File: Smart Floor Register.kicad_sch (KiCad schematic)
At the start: 0 parts

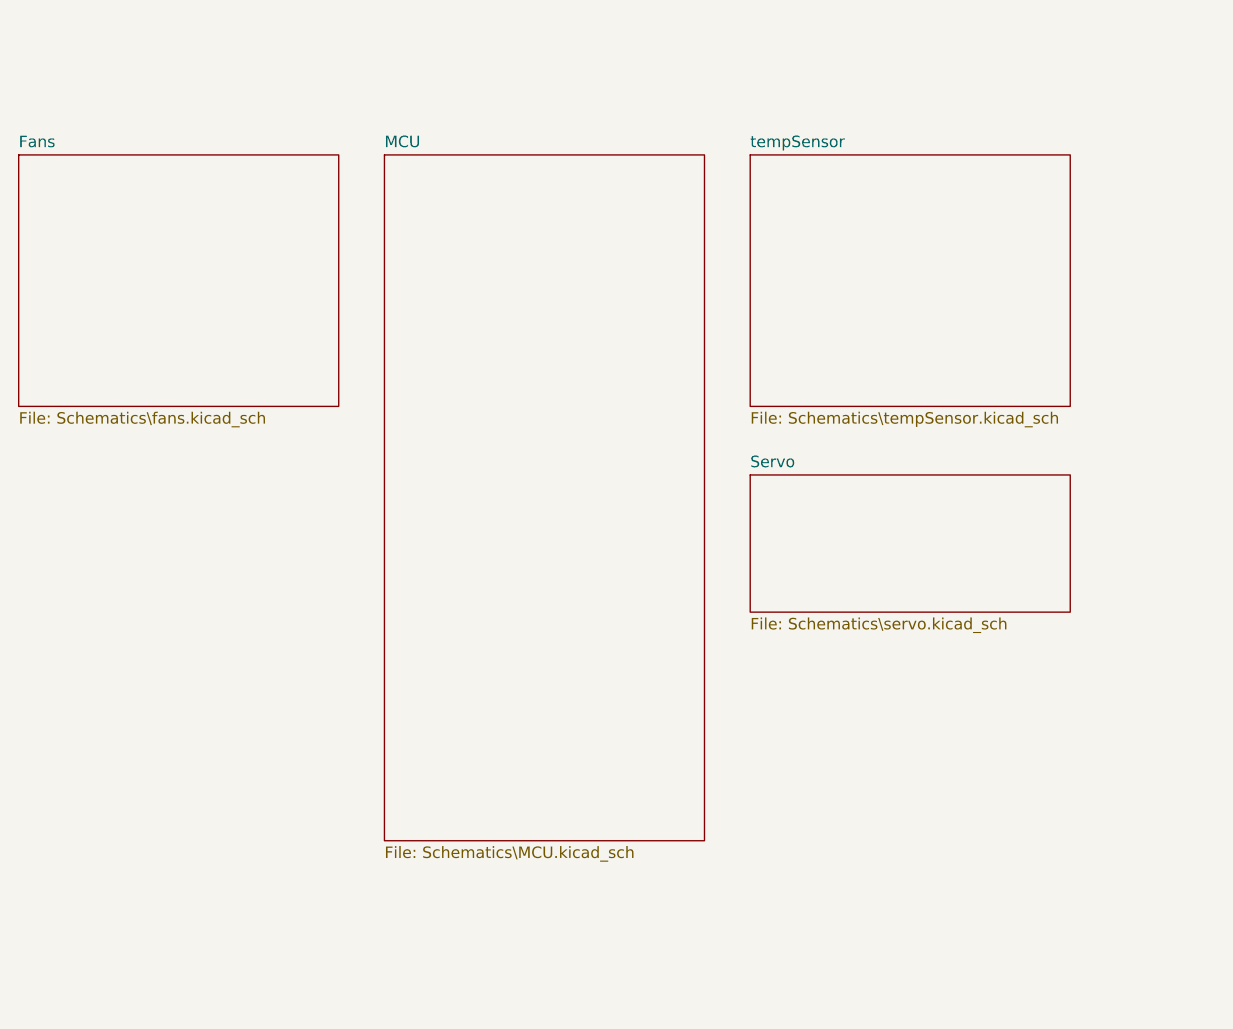
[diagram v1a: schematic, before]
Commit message: Add MCU circuit
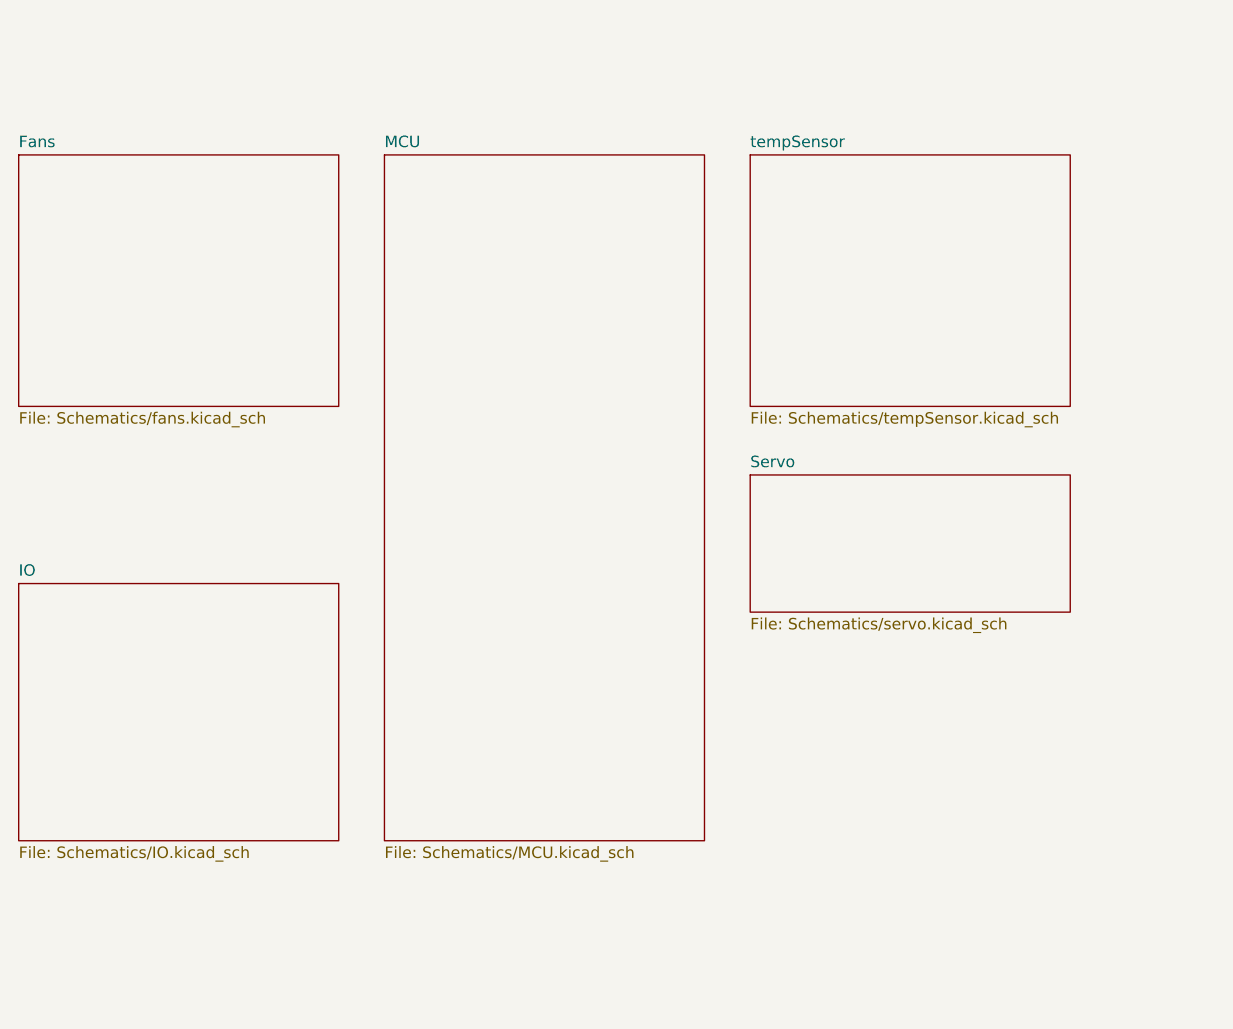
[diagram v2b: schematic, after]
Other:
- added sheet IO (Schematics/IO.kicad_sch)
- sheet Fans: file Schematics\fans.kicad_sch -> Schematics/fans.kicad_sch
- sheet MCU: file Schematics\MCU.kicad_sch -> Schematics/MCU.kicad_sch
- sheet Servo: file Schematics\servo.kicad_sch -> Schematics/servo.kicad_sch
- sheet tempSensor: file Schematics\tempSensor.kicad_sch -> Schematics/tempSensor.kicad_sch
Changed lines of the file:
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@@
       (effects (font (size 1.27 1.27)) (justify left bottom))
     )
-    (property "Sheet file" "Schematics\\servo.kicad_sch" (id 1) (at 165.1 114.8846 0)
+    (property "Sheet file" "Schematics/servo.kicad_sch" (id 1) (at 165.1 114.8846 0)
       (effects (font (size 1.27 1.27)) (justify left top))
     )
@@
       (effects (font (size 1.27 1.27)) (justify left bottom))
     )
-    (property "Sheet file" "Schematics\\MCU.kicad_sch" (id 1) (at 124.46 140.2846 0)
+    (property "Sheet file" "Schematics/MCU.kicad_sch" (id 1) (at 124.46 140.2846 0)
       (effects (font (size 1.27 1.27)) (justify left top))
     )
@@
       (effects (font (size 1.27 1.27)) (justify left bottom))
     )
-    (property "Sheet file" "Schematics\\tempSensor.kicad_sch" (id 1) (at 165.1 92.0246 0)
+    (property "Sheet file" "Schematics/tempSensor.kicad_sch" (id 1) (at 165.1 92.0246 0)
+      (effects (font (size 1.27 1.27)) (justify left top))
+    )
+  )
+  (sheet (at 83.82 111.125) (size 35.56 28.575) (fields_autoplaced)
+    (stroke (width 0.1524) (type solid) (color 0 0 0 0))
+    (fill (color 0 0 0 0.0000))
+    (property "Sheet name" "IO" (id 0) (at 83.82 110.4134 0)
+      (effects (font (size 1.27 1.27)) (justify left bottom))
+    )
+    (property "Sheet file" "Schematics/IO.kicad_sch" (id 1) (at 83.82 140.2846 0)
       (effects (font (size 1.27 1.27)) (justify left top))
     )
@@
       (effects (font (size 1.27 1.27)) (justify left bottom))
     )
-    (property "Sheet file" "Schematics\\fans.kicad_sch" (id 1) (at 83.82 92.0246 0)
+    (property "Sheet file" "Schematics/fans.kicad_sch" (id 1) (at 83.82 92.0246 0)
       (effects (font (size 1.27 1.27)) (justify left top))
     )
@@
     (path "/3b809d5e-1cd6-4bd7-8775-d6e8648b017c" (page "4"))
     (path "/ed227731-8e20-48d6-ab3d-3bb44546ae2c" (page "5"))
+    (path "/e5852d82-8ff6-4012-ac66-763fa215a023" (page "6"))
   )
   (symbol_instances
+    (path "/49126cb1-3295-4f9c-ba5a-a7f1d530269a/0ba5132d-9905-4101-b8fb-d13fd8eb3278"
+      (reference "#PWR?") (unit 1) (value "VCC") (footprint "")
+    )
+    (path "/49126cb1-3295-4f9c-ba5a-a7f1d530269a/33b8dcc0-1a9b-40a0-97ec-c23023a23c96"
+      (reference "#PWR?") (unit 1) (value "Earth") (footprint "")
+    )
+    (path "/49126cb1-3295-4f9c-ba5a-a7f1d530269a/72c0072b-392e-4e7f-97f5-dd28eacd0e25"
+      (reference "#PWR?") (unit 1) (value "Earth") (footprint "")
+    )
+    (path "/49126cb1-3295-4f9c-ba5a-a7f1d530269a/781801cc-7cbe-41ec-88cd-6260168418c2"
+      (reference "#PWR?") (unit 1) (value "Earth") (footprint "")
+    )
+    (path "/49126cb1-3295-4f9c-ba5a-a7f1d530269a/c2f2a113-ef08-4a50-83fd-9e527d0d90f6"
+      (reference "#PWR?") (unit 1) (value "VCC") (footprint "")
+    )
+    (path "/e5852d82-8ff6-4012-ac66-763fa215a023/df26c841-4ff3-4cde-959c-1d6a7c88c93e"
+      (reference "#PWR?") (unit 1) (value "Earth") (footprint "")
+    )
+    (path "/49126cb1-3295-4f9c-ba5a-a7f1d530269a/027587c6-5a8d-4b56-aa6d-ac51c1c0279d"
+      (reference "C?") (unit 1) (value "1uF") (footprint "")
+    )
+    (path "/49126cb1-3295-4f9c-ba5a-a7f1d530269a/317cf53b-7c2d-48ed-ac0b-c02d04fc9aba"
+      (reference "C?") (unit 1) (value "1uF") (footprint "")
+    )
+    (path "/49126cb1-3295-4f9c-ba5a-a7f1d530269a/645e38cc-aaf0-425a-9ead-62a84a8ca331"
+      (reference "C?") (unit 1) (value "1uF") (footprint "")
+    )
+    (path "/e5852d82-8ff6-4012-ac66-763fa215a023/b59f5cd4-3d0b-4837-87b8-455eb74be610"
+      (reference "J?") (unit 1) (value "USB_B_Micro") (footprint "")
+    )
     (path "/49126cb1-3295-4f9c-ba5a-a7f1d530269a/9aa4051b-5d8e-420b-bd92-028862775303"
       (reference "U?") (unit 1) (value "ATmega32U4-M") (footprint "Package_DFN_QFN:QFN-44-1EP_7x7mm_P0.5mm_EP5.2x5.2mm")
     )
+    (path "/49126cb1-3295-4f9c-ba5a-a7f1d530269a/6e0cb104-c4a0-43c8-bedf-8a80f0d18d8f"
+      (reference "Y?") (unit 1) (value "16MHz ") (footprint "")
+    )
   )

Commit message: Motor Controllers
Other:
- added sheet Power (Schematics/power.kicad_sch)
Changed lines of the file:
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@@
 (kicad_sch (version 20211123) (generator eeschema)
   (paper "A4")
-  (sheet (at 165.1 99.06) (size 35.56 15.24) (fields_autoplaced)
+  (sheet (at 171.196 86.614) (size 35.56 15.24) (fields_autoplaced)
     (stroke (width 0.1524) (type solid) (color 0 0 0 0))
     (fill (color 0 0 0 0.0000))
-    (property "Sheet name" "Servo" (id 0) (at 165.1 98.3484 0)
+    (property "Sheet name" "Servo" (id 0) (at 171.196 85.9024 0)
       (effects (font (size 1.27 1.27)) (justify left bottom))
     )
-    (property "Sheet file" "Schematics/servo.kicad_sch" (id 1) (at 165.1 114.8846 0)
+    (property "Sheet file" "Schematics/servo.kicad_sch" (id 1) (at 171.196 102.4386 0)
       (effects (font (size 1.27 1.27)) (justify left top))
     )
   )
-  (sheet (at 124.46 63.5) (size 35.56 76.2) (fields_autoplaced)
+  (sheet (at 130.556 51.054) (size 35.56 76.2) (fields_autoplaced)
     (stroke (width 0.1524) (type solid) (color 0 0 0 0))
     (fill (color 0 0 0 0.0000))
-    (property "Sheet name" "MCU" (id 0) (at 124.46 62.7884 0)
+    (property "Sheet name" "MCU" (id 0) (at 130.556 50.3424 0)
       (effects (font (size 1.27 1.27)) (justify left bottom))
     )
-    (property "Sheet file" "Schematics/MCU.kicad_sch" (id 1) (at 124.46 140.2846 0)
+    (property "Sheet file" "Schematics/MCU.kicad_sch" (id 1) (at 130.556 127.8386 0)
       (effects (font (size 1.27 1.27)) (justify left top))
     )
   )
-  (sheet (at 165.1 63.5) (size 35.56 27.94) (fields_autoplaced)
+  (sheet (at 171.196 51.054) (size 35.56 27.94) (fields_autoplaced)
     (stroke (width 0.1524) (type solid) (color 0 0 0 0))
     (fill (color 0 0 0 0.0000))
-    (property "Sheet name" "tempSensor" (id 0) (at 165.1 62.7884 0)
+    (property "Sheet name" "tempSensor" (id 0) (at 171.196 50.3424 0)
       (effects (font (size 1.27 1.27)) (justify left bottom))
     )
-    (property "Sheet file" "Schematics/tempSensor.kicad_sch" (id 1) (at 165.1 92.0246 0)
+    (property "Sheet file" "Schematics/tempSensor.kicad_sch" (id 1) (at 171.196 79.5786 0)
       (effects (font (size 1.27 1.27)) (justify left top))
     )
   )
-  (sheet (at 83.82 111.125) (size 35.56 28.575) (fields_autoplaced)
+  (sheet (at 89.916 98.679) (size 35.56 28.575) (fields_autoplaced)
     (stroke (width 0.1524) (type solid) (color 0 0 0 0))
     (fill (color 0 0 0 0.0000))
-    (property "Sheet name" "IO" (id 0) (at 83.82 110.4134 0)
+    (property "Sheet name" "IO" (id 0) (at 89.916 97.9674 0)
       (effects (font (size 1.27 1.27)) (justify left bottom))
     )
-    (property "Sheet file" "Schematics/IO.kicad_sch" (id 1) (at 83.82 140.2846 0)
+    (property "Sheet file" "Schematics/IO.kicad_sch" (id 1) (at 89.916 127.8386 0)
       (effects (font (size 1.27 1.27)) (justify left top))
     )
   )
-  (sheet (at 83.82 63.5) (size 35.56 27.94) (fields_autoplaced)
+  (sheet (at 89.916 51.054) (size 35.56 27.94) (fields_autoplaced)
     (stroke (width 0.1524) (type solid) (color 0 0 0 0))
     (fill (color 0 0 0 0.0000))
-    (property "Sheet name" "Fans" (id 0) (at 83.82 62.7884 0)
+    (property "Sheet name" "Fans" (id 0) (at 89.916 50.3424 0)
       (effects (font (size 1.27 1.27)) (justify left bottom))
     )
-    (property "Sheet file" "Schematics/fans.kicad_sch" (id 1) (at 83.82 92.0246 0)
+    (property "Sheet file" "Schematics/fans.kicad_sch" (id 1) (at 89.916 79.5786 0)
+      (effects (font (size 1.27 1.27)) (justify left top))
+    )
+  )
+  (sheet (at 130.556 134.112) (size 35.56 21.844) (fields_autoplaced)
+    (stroke (width 0.1524) (type solid) (color 0 0 0 0))
+    (fill (color 0 0 0 0.0000))
+    (property "Sheet name" "Power" (id 0) (at 130.556 133.4004 0)
+      (effects (font (size 1.27 1.27)) (justify left bottom))
+    )
+    (property "Sheet file" "Schematics/power.kicad_sch" (id 1) (at 130.556 156.5406 0)
       (effects (font (size 1.27 1.27)) (justify left top))
     )
@@
     (path "/ed227731-8e20-48d6-ab3d-3bb44546ae2c" (page "5"))
     (path "/e5852d82-8ff6-4012-ac66-763fa215a023" (page "6"))
+    (path "/f99fd107-6bfd-4782-b1b5-5fe450dca1f7" (page "7"))
   )
   (symbol_instances
@@
       (reference "#PWR?") (unit 1) (value "VCC") (footprint "")
     )
+    (path "/ed227731-8e20-48d6-ab3d-3bb44546ae2c/2eaf935d-6fe0-415a-b628-4afda34a3729"
+      (reference "#PWR?") (unit 1) (value "Earth") (footprint "")
+    )
     (path "/49126cb1-3295-4f9c-ba5a-a7f1d530269a/33b8dcc0-1a9b-40a0-97ec-c23023a23c96"
       (reference "#PWR?") (unit 1) (value "Earth") (footprint "")
+    )
+    (path "/ed227731-8e20-48d6-ab3d-3bb44546ae2c/4a5a473b-3acc-4b18-a2fe-3193466d9748"
+      (reference "#PWR?") (unit 1) (value "Earth") (footprint "")
+    )
+    (path "/ed227731-8e20-48d6-ab3d-3bb44546ae2c/65d251b2-2212-435d-ace5-d3202658cc1c"
+      (reference "#PWR?") (unit 1) (value "+5V") (footprint "")
     )
     (path "/49126cb1-3295-4f9c-ba5a-a7f1d530269a/72c0072b-392e-4e7f-97f5-dd28eacd0e25"
@@
       (reference "#PWR?") (unit 1) (value "Earth") (footprint "")
     )
+    (path "/ed227731-8e20-48d6-ab3d-3bb44546ae2c/93434a0d-4343-42da-807b-451ad6c10233"
+      (reference "#PWR?") (unit 1) (value "Earth") (footprint "")
+    )
     (path "/e5852d82-8ff6-4012-ac66-763fa215a023/a069176b-4e6a-428d-afef-40f4b660b3d0"
       (reference "#PWR?") (unit 1) (value "Earth") (footprint "")
+    )
+    (path "/ed227731-8e20-48d6-ab3d-3bb44546ae2c/b2d40495-13c3-4fbc-8c95-fe292f91a46d"
+      (reference "#PWR?") (unit 1) (value "+5V") (footprint "")
     )
     (path "/49126cb1-3295-4f9c-ba5a-a7f1d530269a/c2f2a113-ef08-4a50-83fd-9e527d0d90f6"
@@
     )
     (path "/e5852d82-8ff6-4012-ac66-763fa215a023/df26c841-4ff3-4cde-959c-1d6a7c88c93e"
+      (reference "#PWR?") (unit 1) (value "Earth") (footprint "")
+    )
+    (path "/ed227731-8e20-48d6-ab3d-3bb44546ae2c/f0ae2c0f-21b7-4a36-ae53-b8648cae5dfc"
       (reference "#PWR?") (unit 1) (value "Earth") (footprint "")
     )
@@
       (reference "C?") (unit 1) (value "1uF") (footprint "")
     )
+    (path "/ed227731-8e20-48d6-ab3d-3bb44546ae2c/40418568-e52f-48a6-839f-94a9ff29a7e1"
+      (reference "C?") (unit 1) (value "10uF") (footprint "")
+    )
     (path "/49126cb1-3295-4f9c-ba5a-a7f1d530269a/645e38cc-aaf0-425a-9ead-62a84a8ca331"
       (reference "C?") (unit 1) (value "1uF") (footprint "")
+    )
+    (path "/ed227731-8e20-48d6-ab3d-3bb44546ae2c/825e29db-3e48-4d07-97c7-aed2fe976037"
+      (reference "C?") (unit 1) (value "10uF") (footprint "")
+    )
+    (path "/ed227731-8e20-48d6-ab3d-3bb44546ae2c/64f19276-20a8-40cb-9fbd-736ace904ff8"
+      (reference "J?") (unit 1) (value "Fan 1") (footprint "")
     )
     (path "/e5852d82-8ff6-4012-ac66-763fa215a023/b59f5cd4-3d0b-4837-87b8-455eb74be610"
       (reference "J?") (unit 1) (value "USB_B_Micro") (footprint "")
     )
+    (path "/ed227731-8e20-48d6-ab3d-3bb44546ae2c/fcf8fbd6-acf2-4902-bd1e-a7ddf8143905"
+      (reference "J?") (unit 1) (value "Fan 2") (footprint "")
+    )
     (path "/e5852d82-8ff6-4012-ac66-763fa215a023/2ca6adc3-32cf-4a09-99ec-7132fa9b0804"
       (reference "R?") (unit 1) (value "0R") (footprint "")
+    )
+    (path "/ed227731-8e20-48d6-ab3d-3bb44546ae2c/19543dc7-cb66-4f5f-b434-d18ff8123534"
+      (reference "U?") (unit 1) (value "LTC1695") (footprint "")
     )
     (path "/49126cb1-3295-4f9c-ba5a-a7f1d530269a/9aa4051b-5d8e-420b-bd92-028862775303"
       (reference "U?") (unit 1) (value "ATmega32U4-M") (footprint "Package_DFN_QFN:QFN-44-1EP_7x7mm_P0.5mm_EP5.2x5.2mm")
     )
+    (path "/ed227731-8e20-48d6-ab3d-3bb44546ae2c/f2ead17b-0ba9-439d-ac17-1f65ee51c09d"
+      (reference "U?") (unit 1) (value "LTC1695") (footprint "")
+    )
     (path "/49126cb1-3295-4f9c-ba5a-a7f1d530269a/6e0cb104-c4a0-43c8-bedf-8a80f0d18d8f"

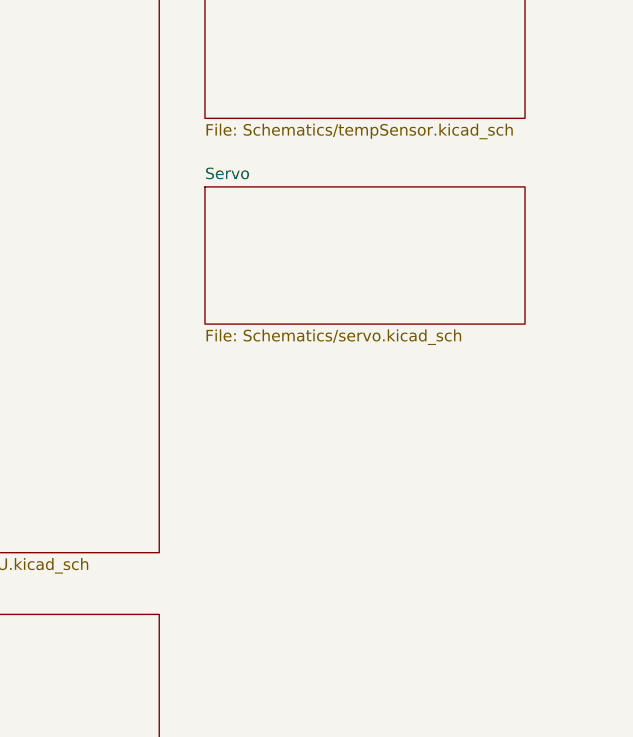
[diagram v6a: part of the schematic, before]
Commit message: Changed MCU
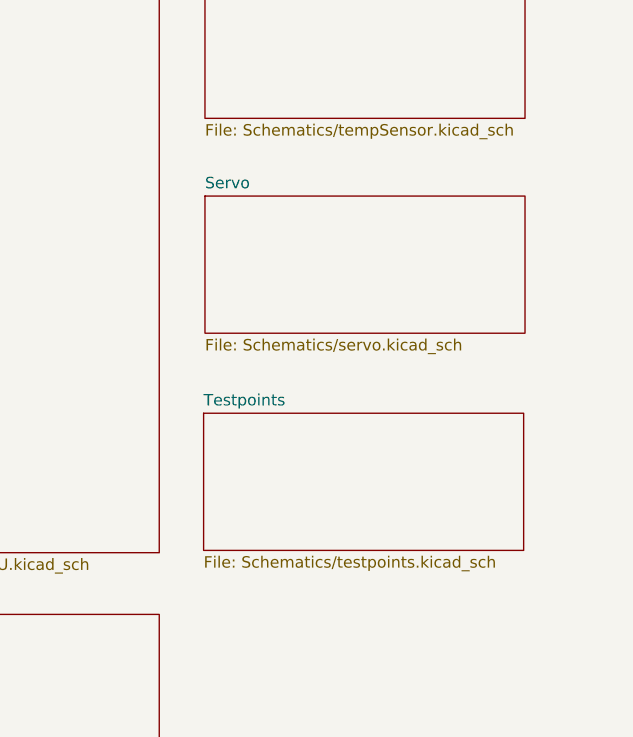
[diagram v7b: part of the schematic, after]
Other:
- added sheet Testpoints (Schematics/testpoints.kicad_sch)
